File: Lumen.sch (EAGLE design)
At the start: 33 parts, among them J1 AVR_SPI_PRG_6PTH, U1 Tiny45-20-SMT, Y1 8Mhz

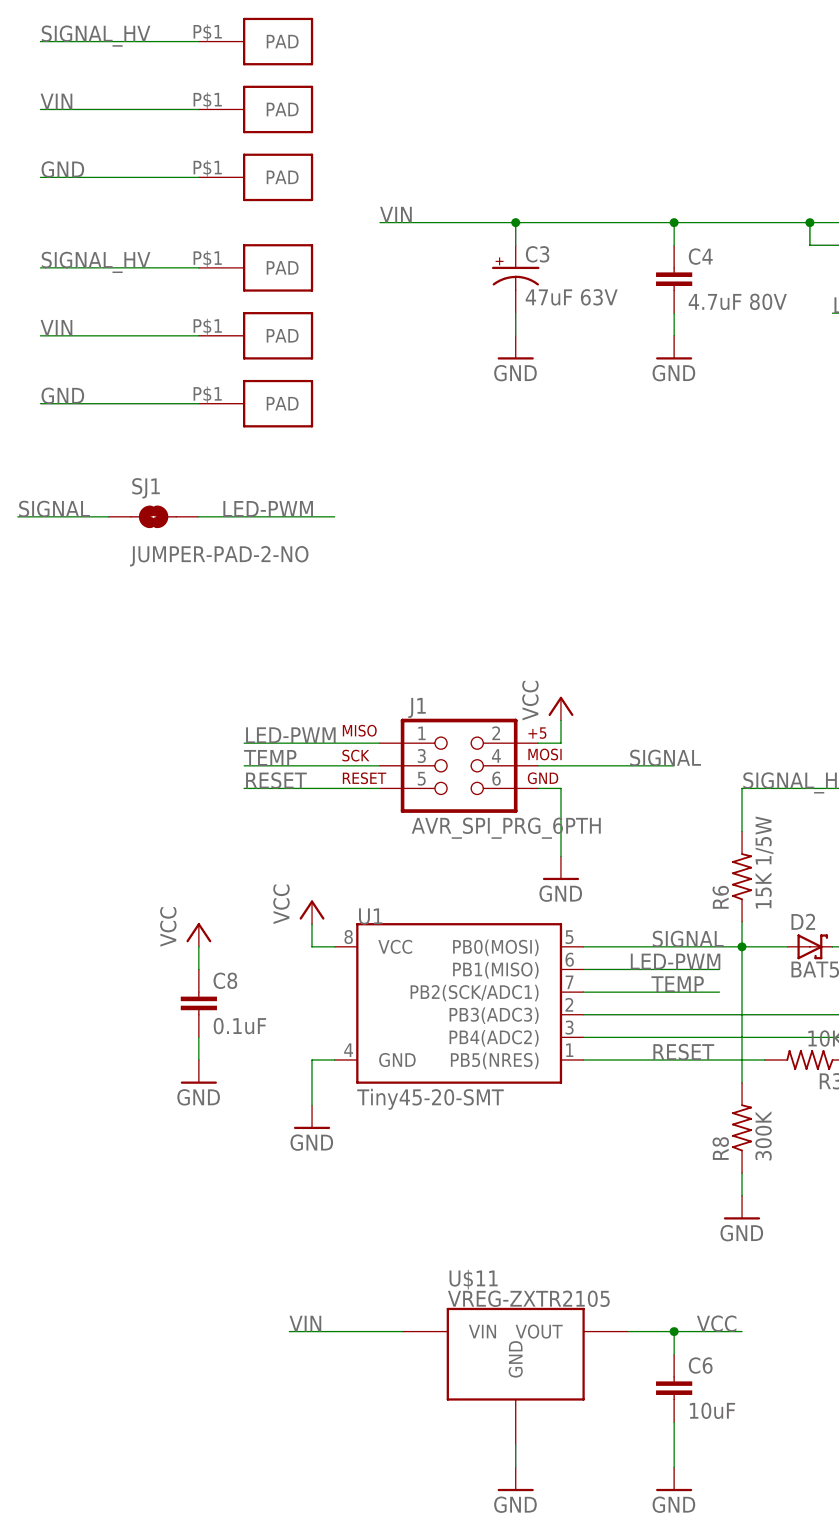
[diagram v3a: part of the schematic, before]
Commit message: Rev6 as produced with IDC connector.
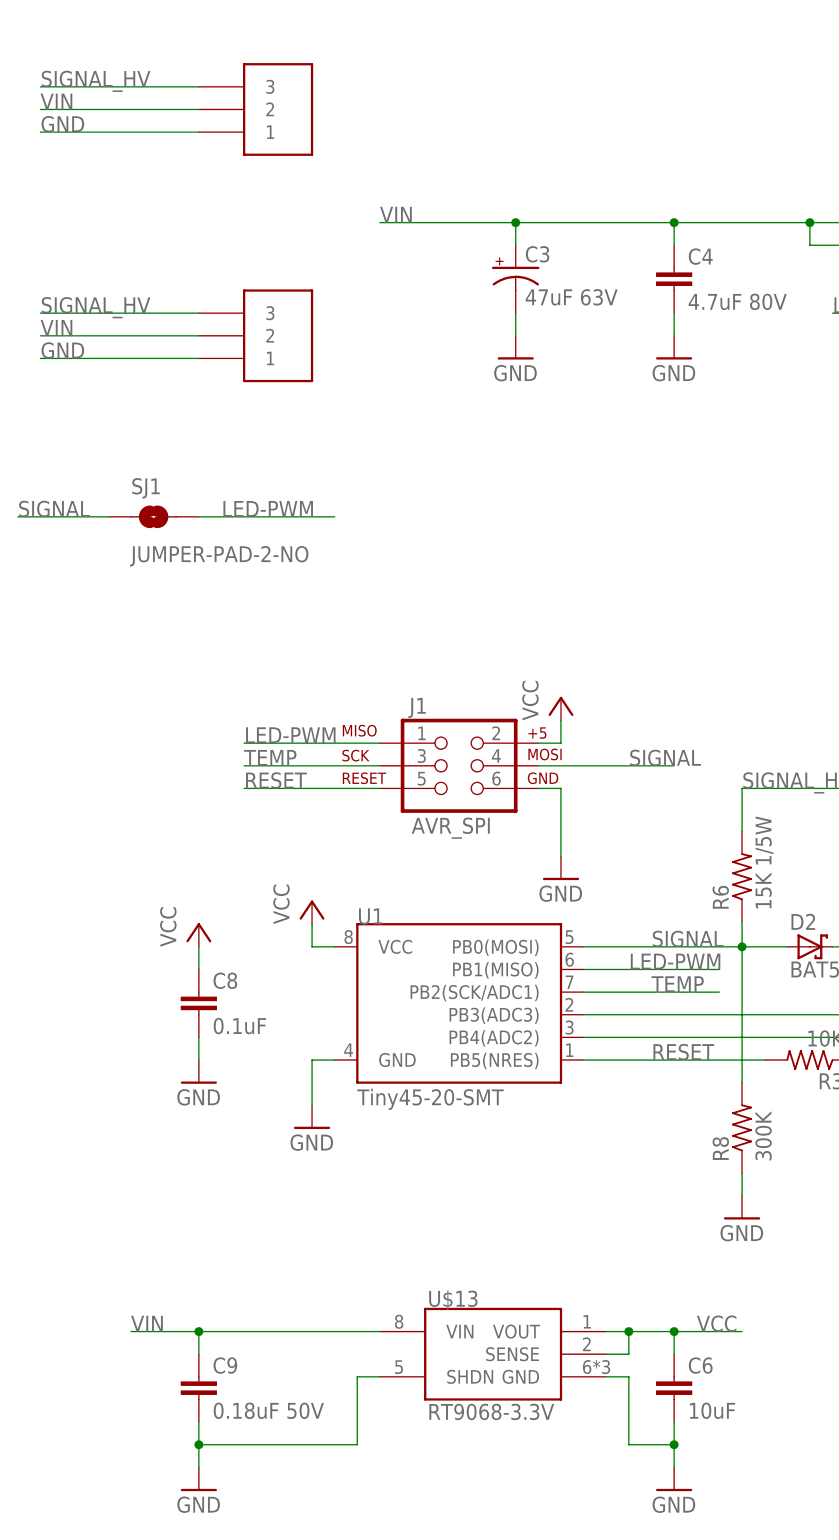
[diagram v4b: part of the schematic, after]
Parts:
- removed U$4, U$5, U$6, U$7, U$8, U$9: PAD2X3MM, BlueRobotics-Main:PAD2X3MM
- added C9: 0.18uF 50V, resistor:C-EUC0805
- added U$12: 009176003032006, BlueRobotics-Main:HEADER-3AVX-9176
- added U$13: RT9068-3.3V, BlueRobotics-Main:VREG-RT9068SOP-8
- J1: value AVR_SPI_PRG_6PTH -> AVR_SPI
- U$11: value VREG-ZXTR2105 -> 009176003032006; device BlueRobotics-Main:VREG-ZXTR2105 -> BlueRobotics-Main:HEADER-3AVX-9176
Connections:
- net GND: now also C9.2, U$11.1, U$12.1, U$13.GND, U$13.SHDN; no longer U$11.GND, U$6.PAD, U$9.PAD
- net SIGNAL_HV: now also U$11.3, U$12.3; no longer U$4.PAD, U$7.PAD
- net VCC: now also U$13.SENSE, U$13.VOUT; no longer U$11.VOUT
- net VIN: now also C9.1, U$11.2, U$12.2, U$13.VIN; no longer U$11.VIN, U$5.PAD, U$8.PAD
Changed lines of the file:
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@@
 <part name="R3" library="resistor" deviceset="R-US_" device="R0603" value="10K"/>
 <part name="GND4" library="supply1" deviceset="GND" device=""/>
-<part name="J1" library="SparkFun-Connectors" deviceset="AVR_SPI_PRG_6" device="PTH"/>
-<part name="U$4" library="BlueRobotics-Main" deviceset="PAD" device="2X3MM" value="PAD2X3MM"/>
-<part name="U$5" library="BlueRobotics-Main" deviceset="PAD" device="2X3MM" value="PAD2X3MM"/>
-<part name="U$6" library="BlueRobotics-Main" deviceset="PAD" device="2X3MM" value="PAD2X3MM"/>
-<part name="U$7" library="BlueRobotics-Main" deviceset="PAD" device="2X3MM" value="PAD2X3MM"/>
-<part name="U$8" library="BlueRobotics-Main" deviceset="PAD" device="2X3MM" value="PAD2X3MM"/>
-<part name="U$9" library="BlueRobotics-Main" deviceset="PAD" device="2X3MM" value="PAD2X3MM"/>
+<part name="J1" library="SparkFun-Connectors" deviceset="AVR_SPI_PRG_6" device="PTH" value="AVR_SPI"/>
 <part name="R4" library="resistor" deviceset="R-US_" device="R0603" value="3.3K 1%"/>
 <part name="R5" library="resistor" deviceset="R-US_" device="R0603" value="10K NTC"/>
@@
 <part name="GND8" library="supply1" deviceset="GND" device=""/>
 <part name="U$10" library="BlueRobotics-Main" deviceset="LOGO" device="BR-LOGO-MS-COPPER" value="LOGOBR-LOGO-MS-COPPER"/>
-<part name="U$11" library="BlueRobotics-Main" deviceset="VREG-ZXTR2105" device=""/>
-<part name="GND11" library="supply1" deviceset="GND" device=""/>
 <part name="C6" library="resistor" deviceset="C-EU" device="C0603" value="10uF"/>
 <part name="GND13" library="supply1" deviceset="GND" device=""/>
@@
 <part name="R8" library="BlueRobotics-Main" deviceset="RESISTOR" device="_0402" value="300K"/>
 <part name="Y1" library="SparkFun" deviceset="RESONATOR" device="SMD" value="8Mhz"/>
+<part name="U$13" library="BlueRobotics-Main" deviceset="VREG-RT9068" device="SOP-8" value="RT9068-3.3V"/>
+<part name="C9" library="resistor" deviceset="C-EU" device="C0805" value="0.18uF 50V"/>
+<part name="GND11" library="supply1" deviceset="GND" device=""/>
+<part name="U$11" library="BlueRobotics-Main" deviceset="HEADER-3" device="AVX-9176" value="009176003032006"/>
+<part name="U$12" library="BlueRobotics-Main" deviceset="HEADER-3" device="AVX-9176" value="009176003032006"/>
 </parts>
 <sheets>
@@
 <instance part="GND4" gate="1" x="40.64" y="53.34"/>
 <instance part="J1" gate="G$1" x="55.88" y="93.98"/>
-<instance part="U$4" gate="G$1" x="33.02" y="175.26"/>
-<instance part="U$5" gate="G$1" x="33.02" y="167.64"/>
-<instance part="U$6" gate="G$1" x="33.02" y="160.02"/>
-<instance part="U$7" gate="G$1" x="33.02" y="149.86"/>
-<instance part="U$8" gate="G$1" x="33.02" y="142.24"/>
-<instance part="U$9" gate="G$1" x="33.02" y="134.62"/>
 <instance part="R4" gate="G$1" x="165.1" y="73.66" rot="R90"/>
 <instance part="R5" gate="G$1" x="165.1" y="55.88" rot="R90"/>
@@
 <instance part="GND8" gate="1" x="132.08" y="53.34"/>
 <instance part="U$10" gate="G$1" x="226.06" y="33.02"/>
-<instance part="U$11" gate="G$1" x="63.5" y="25.4"/>
-<instance part="GND11" gate="1" x="63.5" y="12.7"/>
 <instance part="C6" gate="G$1" x="81.28" y="25.4"/>
 <instance part="GND13" gate="1" x="81.28" y="12.7"/>
@@
 <instance part="R8" gate="G$1" x="88.9" y="53.34" rot="R90"/>
 <instance part="Y1" gate="G$1" x="121.92" y="66.04" rot="R90"/>
+<instance part="U$13" gate="G$1" x="53.34" y="22.86"/>
+<instance part="C9" gate="G$1" x="27.94" y="25.4"/>
+<instance part="GND11" gate="1" x="27.94" y="12.7"/>
+<instance part="U$11" gate="G$1" x="40.64" y="172.72" rot="R180"/>
+<instance part="U$12" gate="G$1" x="40.64" y="147.32" rot="R180"/>
 </instances>
 <busses>
@@
 </segment>
 <segment>
-<pinref part="U$6" gate="G$1" pin="PAD"/>
-<wire x1="27.94" y1="160.02" x2="10.16" y2="160.02" width="0.1524" layer="91"/>
-<label x="10.16" y="160.02" size="1.778" layer="95"/>
-</segment>
-<segment>
-<pinref part="U$9" gate="G$1" pin="PAD"/>
-<wire x1="27.94" y1="134.62" x2="10.16" y2="134.62" width="0.1524" layer="91"/>
-<label x="10.16" y="134.62" size="1.778" layer="95"/>
+<wire x1="27.94" y1="165.1" x2="10.16" y2="165.1" width="0.1524" layer="91"/>
+<label x="10.16" y="165.1" size="1.778" layer="95"/>
+<pinref part="U$11" gate="G$1" pin="1"/>
+</segment>
+<segment>
+<wire x1="27.94" y1="139.7" x2="10.16" y2="139.7" width="0.1524" layer="91"/>
+<label x="10.16" y="139.7" size="1.778" layer="95"/>
+<pinref part="U$12" gate="G$1" pin="1"/>
 </segment>
 <segment>
@@
 </segment>
 <segment>
-<pinref part="GND11" gate="1" pin="GND"/>
-<pinref part="U$11" gate="G$1" pin="GND"/>
-<wire x1="63.5" y1="15.24" x2="63.5" y2="17.78" width="0.1524" layer="91"/>
-</segment>
-<segment>
 <pinref part="GND13" gate="1" pin="GND"/>
 <pinref part="C6" gate="G$1" pin="2"/>
-<wire x1="81.28" y1="15.24" x2="81.28" y2="20.32" width="0.1524" layer="91"/>
+<wire x1="81.28" y1="15.24" x2="81.28" y2="17.78" width="0.1524" layer="91"/>
+<pinref part="U$13" gate="G$1" pin="GND"/>
+<wire x1="81.28" y1="17.78" x2="81.28" y2="20.32" width="0.1524" layer="91"/>
+<wire x1="73.66" y1="25.4" x2="76.2" y2="25.4" width="0.1524" layer="91"/>
+<wire x1="76.2" y1="25.4" x2="76.2" y2="17.78" width="0.1524" layer="91"/>
+<wire x1="76.2" y1="17.78" x2="81.28" y2="17.78" width="0.1524" layer="91"/>
+<junction x="81.28" y="17.78"/>
 </segment>
 <segment>
@@
 <pinref part="R8" gate="G$1" pin="1"/>
 <wire x1="88.9" y1="48.26" x2="88.9" y2="45.72" width="0.1524" layer="91"/>
+</segment>
+<segment>
+<pinref part="U$13" gate="G$1" pin="SHDN"/>
+<wire x1="48.26" y1="25.4" x2="45.72" y2="25.4" width="0.1524" layer="91"/>
+<wire x1="45.72" y1="25.4" x2="45.72" y2="17.78" width="0.1524" layer="91"/>
+<pinref part="GND11" gate="1" pin="GND"/>
+<wire x1="45.72" y1="17.78" x2="27.94" y2="17.78" width="0.1524" layer="91"/>
+<wire x1="27.94" y1="17.78" x2="27.94" y2="15.24" width="0.1524" layer="91"/>
+<pinref part="C9" gate="G$1" pin="2"/>
+<wire x1="27.94" y1="17.78" x2="27.94" y2="20.32" width="0.1524" layer="91"/>
+<junction x="27.94" y="17.78"/>
 </segment>
 </net>
@@
 </segment>
 <segment>
-<pinref part="U$5" gate="G$1" pin="PAD"/>
 <wire x1="27.94" y1="167.64" x2="10.16" y2="167.64" width="0.1524" layer="91"/>
 <label x="10.16" y="167.64" size="1.778" layer="95"/>
-</segment>
-<segment>
-<pinref part="U$8" gate="G$1" pin="PAD"/>
+<pinref part="U$11" gate="G$1" pin="2"/>
+</segment>
+<segment>
 <wire x1="27.94" y1="142.24" x2="10.16" y2="142.24" width="0.1524" layer="91"/>
 <label x="10.16" y="142.24" size="1.778" layer="95"/>
-</segment>
-<segment>
-<pinref part="U$11" gate="G$1" pin="VIN"/>
-<wire x1="50.8" y1="30.48" x2="38.1" y2="30.48" width="0.1524" layer="91"/>
-<label x="38.1" y="30.48" size="1.778" layer="95"/>
+<pinref part="U$12" gate="G$1" pin="2"/>
+</segment>
+<segment>
+<wire x1="48.26" y1="30.48" x2="27.94" y2="30.48" width="0.1524" layer="91"/>
+<label x="20.32" y="30.48" size="1.778" layer="95"/>
+<pinref part="U$13" gate="G$1" pin="VIN"/>
+<pinref part="C9" gate="G$1" pin="1"/>
+<wire x1="27.94" y1="30.48" x2="20.32" y2="30.48" width="0.1524" layer="91"/>
+<wire x1="27.94" y1="27.94" x2="27.94" y2="30.48" width="0.1524" layer="91"/>
+<junction x="27.94" y="30.48"/>
 </segment>
 </net>
@@
 </segment>
 <segment>
-<pinref part="U$11" gate="G$1" pin="VOUT"/>
-<wire x1="76.2" y1="30.48" x2="81.28" y2="30.48" width="0.1524" layer="91"/>
+<wire x1="73.66" y1="30.48" x2="76.2" y2="30.48" width="0.1524" layer="91"/>
 <label x="83.82" y="30.48" size="1.778" layer="95"/>
 <pinref part="C6" gate="G$1" pin="1"/>
+<wire x1="76.2" y1="30.48" x2="81.28" y2="30.48" width="0.1524" layer="91"/>
 <wire x1="81.28" y1="30.48" x2="88.9" y2="30.48" width="0.1524" layer="91"/>
 <wire x1="81.28" y1="27.94" x2="81.28" y2="30.48" width="0.1524" layer="91"/>
 <junction x="81.28" y="30.48"/>
+<pinref part="U$13" gate="G$1" pin="VOUT"/>
+<pinref part="U$13" gate="G$1" pin="SENSE"/>
+<wire x1="73.66" y1="27.94" x2="76.2" y2="27.94" width="0.1524" layer="91"/>
+<wire x1="76.2" y1="27.94" x2="76.2" y2="30.48" width="0.1524" layer="91"/>
+<junction x="76.2" y="30.48"/>
 </segment>
 <segment>
@@
 </segment>
 <segment>
-<pinref part="U$7" gate="G$1" pin="PAD"/>
-<wire x1="27.94" y1="149.86" x2="10.16" y2="149.86" width="0.1524" layer="91"/>
-<label x="10.16" y="149.86" size="1.778" layer="95"/>
-</segment>
-<segment>
-<pinref part="U$4" gate="G$1" pin="PAD"/>
-<wire x1="27.94" y1="175.26" x2="10.16" y2="175.26" width="0.1524" layer="91"/>
-<label x="10.16" y="175.26" size="1.778" layer="95"/>
-</segment>
-</net>
+<wire x1="27.94" y1="144.78" x2="10.16" y2="144.78" width="0.1524" layer="91"/>
+<label x="10.16" y="144.78" size="1.778" layer="95"/>
+<pinref part="U$12" gate="G$1" pin="3"/>
+</segment>
+<segment>
+<wire x1="27.94" y1="170.18" x2="10.16" y2="170.18" width="0.1524" layer="91"/>
+<label x="10.16" y="170.18" size="1.778" layer="95"/>
+<pinref part="U$11" gate="G$1" pin="3"/>
+</segment>
+</net>

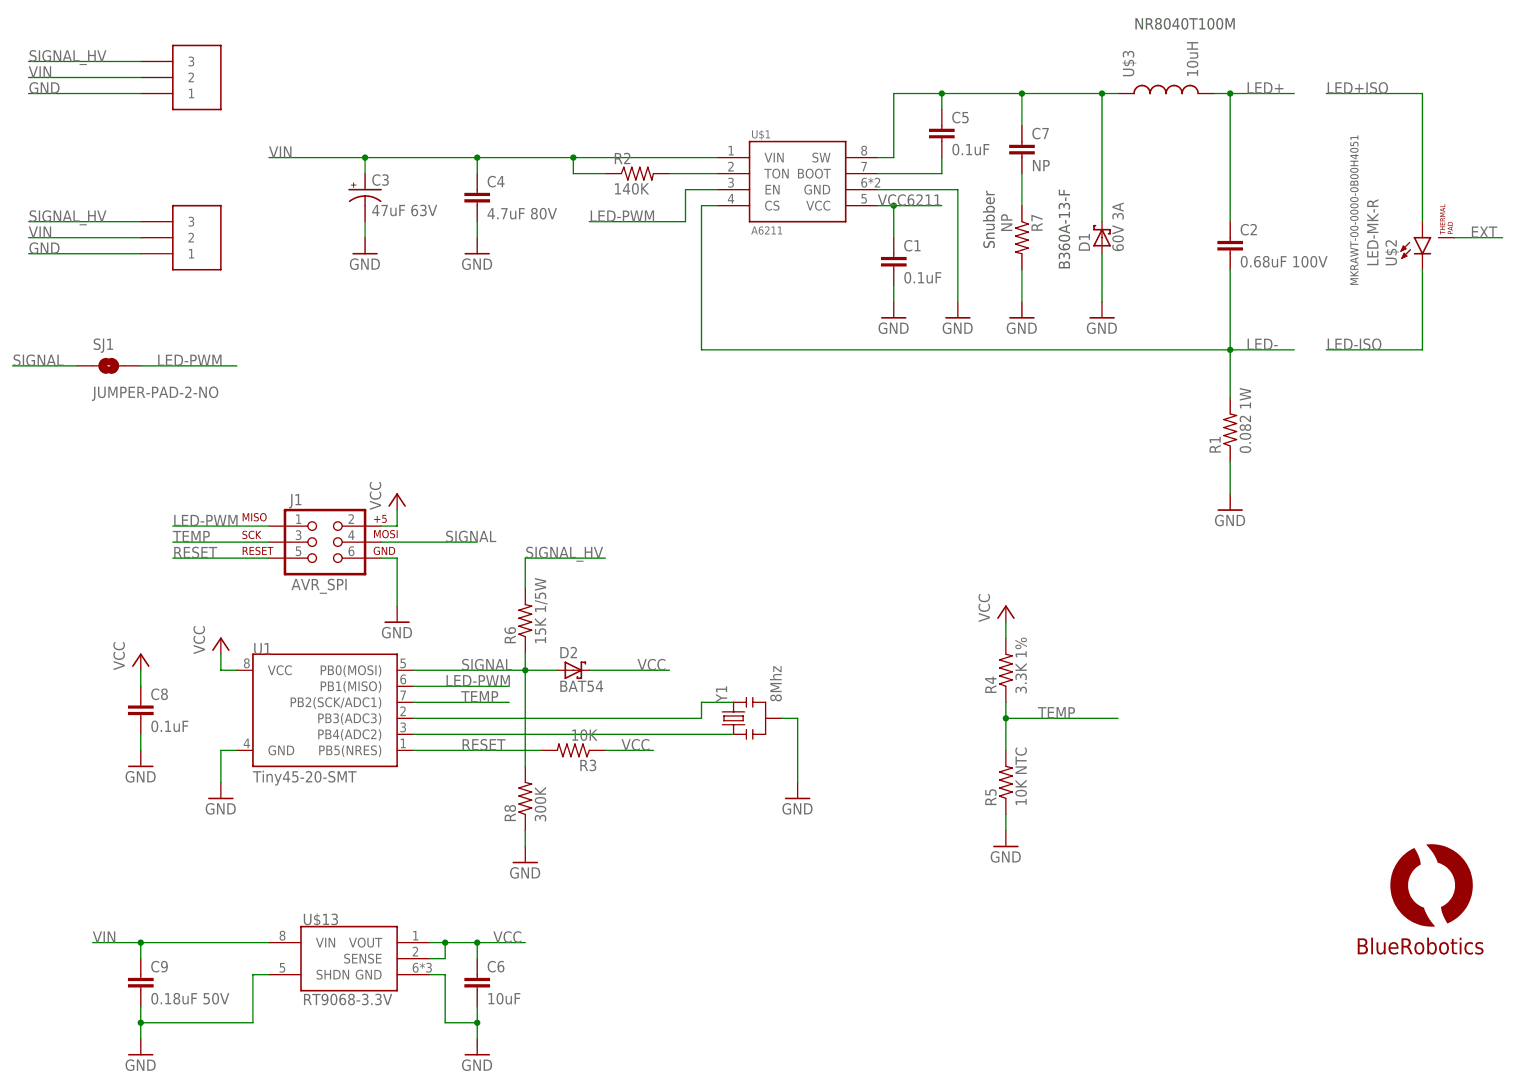
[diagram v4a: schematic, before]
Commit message: Re-layout board for new size. In progress.
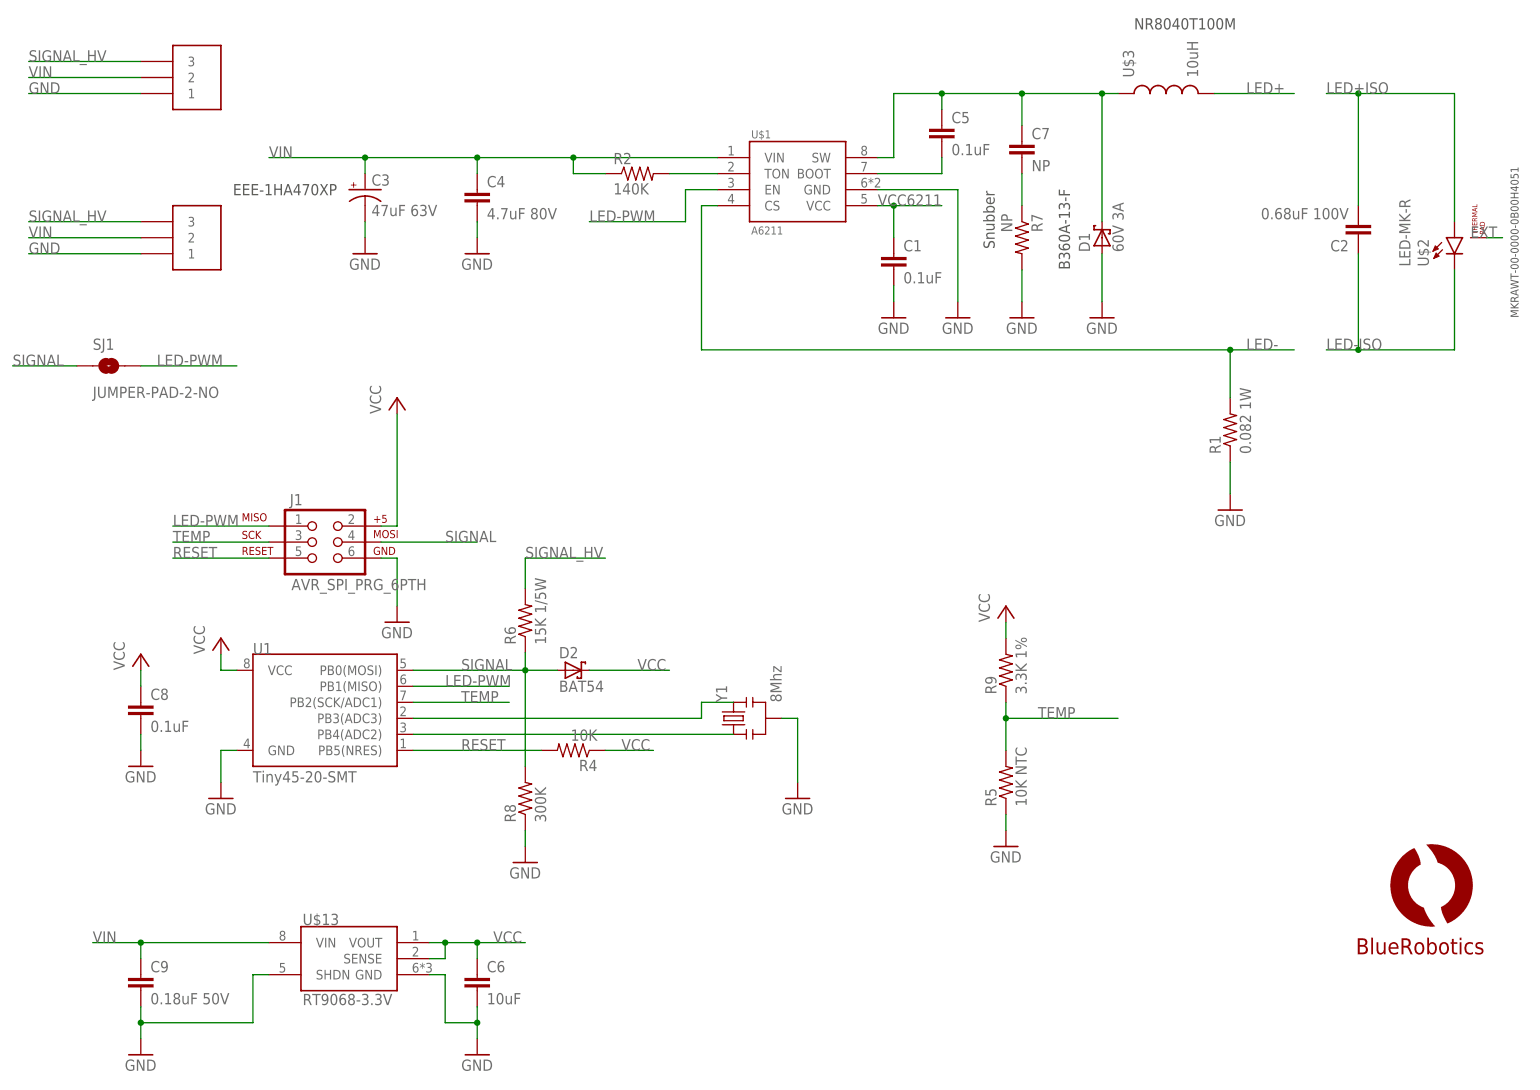
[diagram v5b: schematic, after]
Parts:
- removed R3: 10K, resistor:R-US_R0603
- added R9: 3.3K 1%, BlueRobotics-Main:RESISTOR_0402
- C1, C5, C8: device resistor:C-EUC0603 -> BlueRobotics-Main:CAPACITOR_0402
- C3: device SparkFun-Capacitors:CAP_POLPTH1 -> SparkFun-Capacitors:CAP_POLD
- J1: value AVR_SPI -> AVR_SPI_PRG_6PTH
- R2: device resistor:R-US_R0603 -> BlueRobotics-Main:RESISTOR_0402
- R4: value 3.3K 1% -> 10K; device resistor:R-US_R0603 -> BlueRobotics-Main:RESISTOR_0402
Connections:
- net LED+: no longer C2.1
- net LED+ISO: now also C2.2
- net LED-: no longer C2.2
- net LED-ISO: now also C2.1
- net RESET: now also R4.2; no longer R3.2
- net TEMP: now also R9.1; no longer R4.1
- net VCC: now also R4.1, R9.2; no longer R3.1, R4.2
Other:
- note added: "EEE-1HA470XP"
- moved on the sheet: C2, R4, U$2
